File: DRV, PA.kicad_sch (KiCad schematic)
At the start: 157 parts, among them Q21 2N2222A, Q22 2N2222A, Q23 2N3866, Q24 2N3866, Q25 BD139, Q26 BD139, Q27 2SC5171, Q28 2SA1930, Q29 2SC5171, Q30 2SA1930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

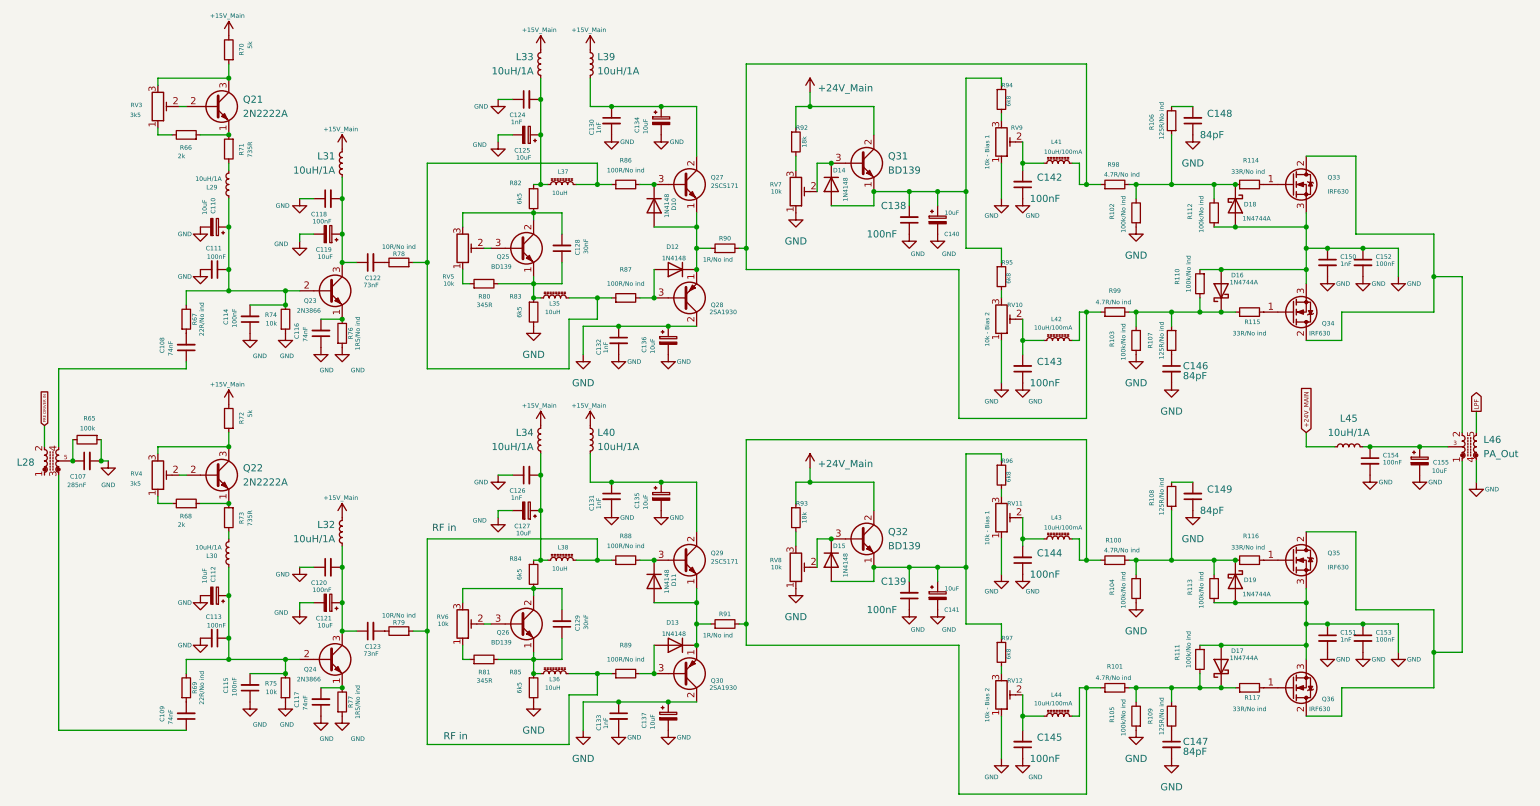
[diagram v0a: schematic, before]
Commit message: Start of testing on LTspice
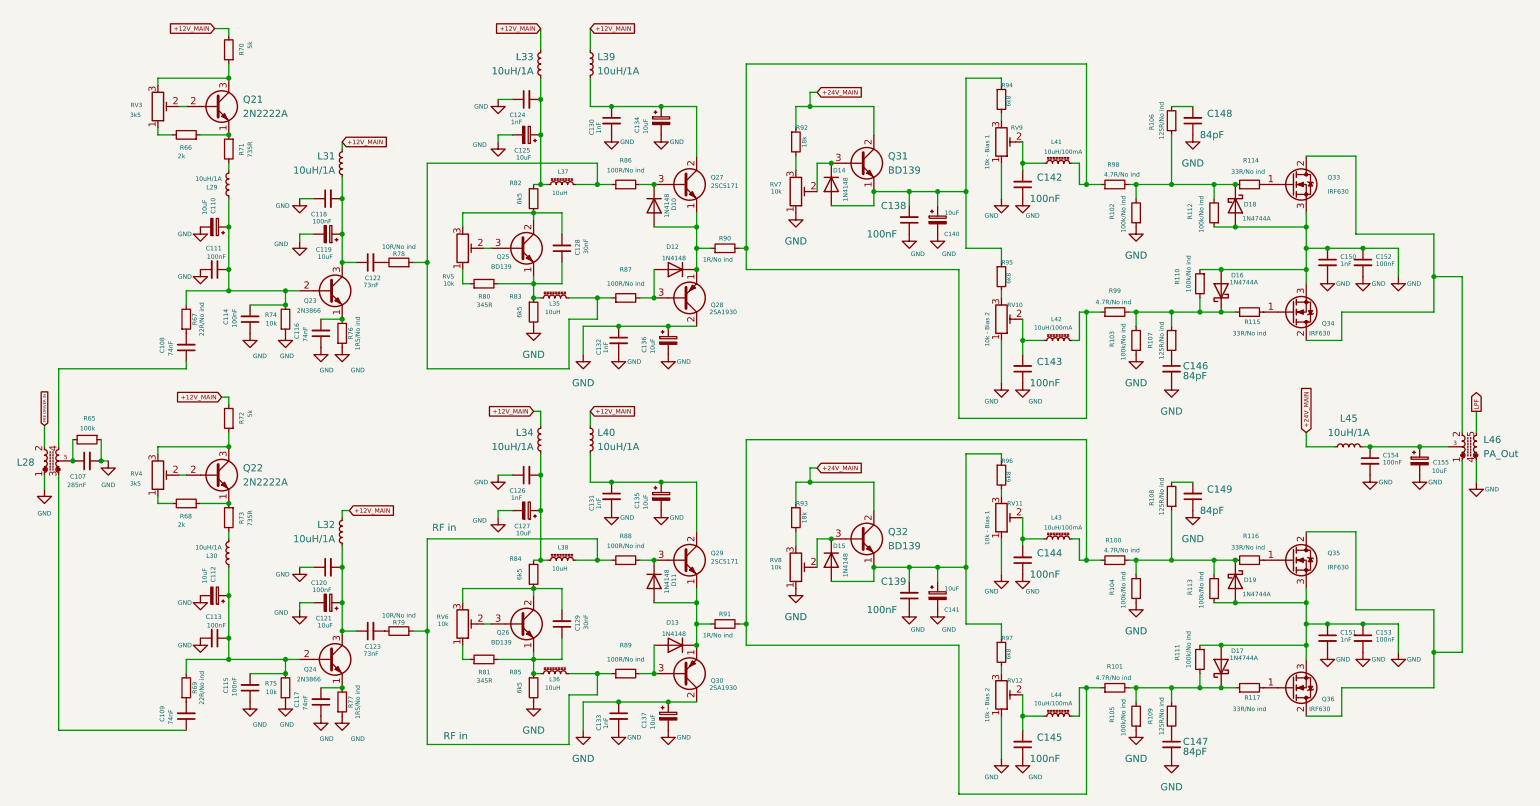
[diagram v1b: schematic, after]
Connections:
- net +24V_Main is gone; now on net +24V_MAIN: Q31.2 (C), Q32.2 (C), R92.1, R93.1
- net GND: now also L28.1
- net +15V_Main renamed +12V_MAIN
